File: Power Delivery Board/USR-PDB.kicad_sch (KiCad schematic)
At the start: 32 parts, among them U1 XT90, U10 Anderson PP45 Vert. 2x1, U11 Anderson PP45 Vert. 2x1, U12 TL2575HV-05IKV, U13 MCP3002-I/P, U2 LM2676T-12_NOPB, U5 Anderson PP45 Vert. 2x1, U6 Anderson PP45 Vert. 2x1, U7 Anderson PP45 Vert. 2x1, U8 Anderson PP45 Vert. 2x1, U9 Anderson PP45 Vert. 2x1

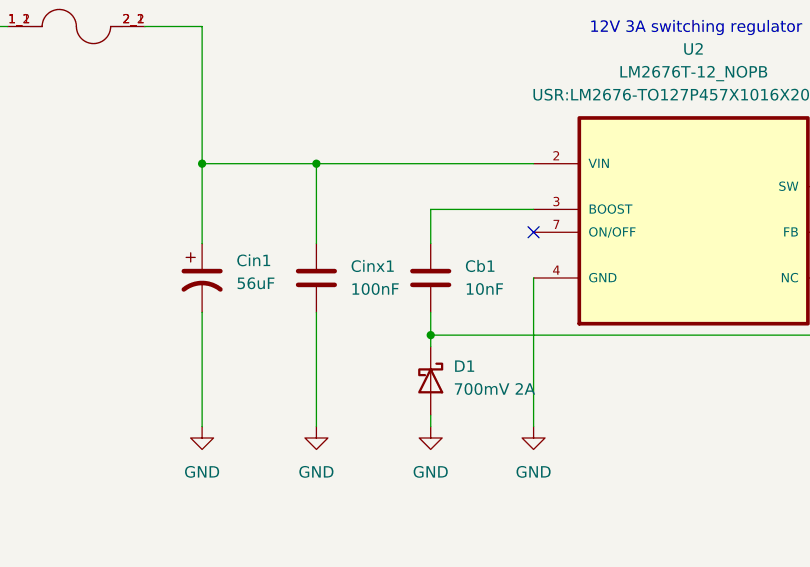
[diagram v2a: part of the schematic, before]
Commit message: Added footprints and datasheets for capacitors, inductors, and diodes
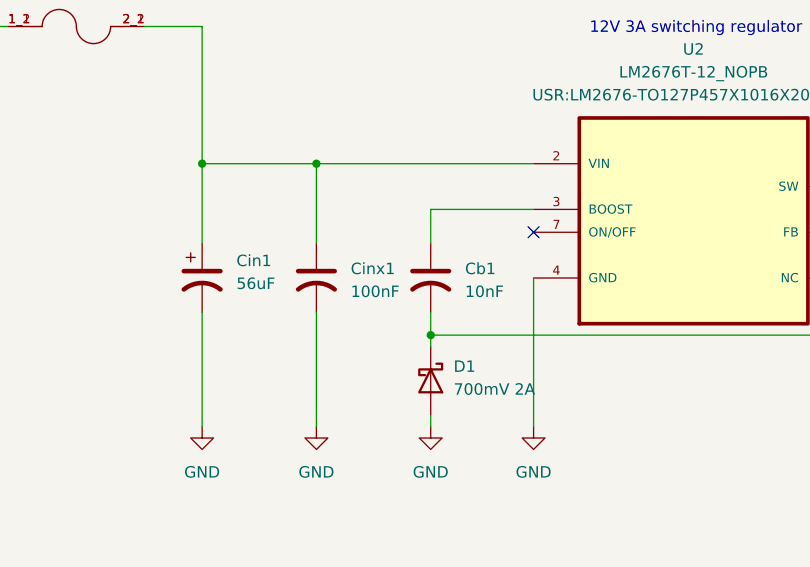
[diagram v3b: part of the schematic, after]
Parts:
- C1, C3: footprint (none) -> USR:U2-K_NCH
- C2: footprint (none) -> USR:PCAP_6.3x7.7-ELECT_NCA
- Cb1, Cinx1: footprint (none) -> USR:CAP_C320C_MOLDED RADIAL_KEM; symbol Device:C -> Device:C_US
- Cin1: footprint (none) -> USR:CAP_WCAP-ATUL_05.0X11.0_WRE
- Cout1: footprint (none) -> USR:CAP_ATLL_06p3X15p0_WRE
- D1: footprint (none) -> USR:SMA_DIO
- L1: footprint (none) -> USR:IND_BOURNS_SRR1210
- L2: footprint (none) -> USR:IND_BOURNS_SDR1806
- L3: footprint (none) -> USR:WE-FI_7447025
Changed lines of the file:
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@@
 			)
 		)
-		(property "Footprint" ""
+		(property "Footprint" "USR:CAP_ATLL_06p3X15p0_WRE"
 			(at 152.4 204.47 0)
 			(effects
@@
 			)
 		)
-		(property "Datasheet" "~"
+		(property "Datasheet" "https://www.we-online.com/components/products/datasheet/860160673019.pdf"
 			(at 152.4 204.47 0)
 			(effects
@@
 			)
 		)
-		(property "Footprint" ""
+		(property "Footprint" "USR:WE-FI_7447025"
 			(at 361.95 210.82 0)
 			(effects
@@
 			)
 		)
-		(property "Footprint" ""
+		(property "Footprint" "USR:PCAP_6.3x7.7-ELECT_NCA"
 			(at 316.23 227.33 0)
 			(effects
@@
 			)
 		)
-		(property "Footprint" ""
+		(property "Footprint" "USR:CAP_WCAP-ATUL_05.0X11.0_WRE"
 			(at 63.5 204.47 0)
 			(effects
@@
 			)
 		)
-		(property "Datasheet" "~"
+		(property "Datasheet" "https://www.we-online.com/components/products/datasheet/860040472002.pdf"
 			(at 63.5 204.47 0)
 			(effects
@@
 			)
 		)
-		(property "Footprint" ""
+		(property "Footprint" "USR:U2-K_NCH"
 			(at 267.97 208.28 0)
 			(effects
@@
 			)
 		)
-		(property "Datasheet" "~"
+		(property "Datasheet" "https://www.nichicon.co.jp/english/series_items/catalog_pdf/e-uud.pdf"
 			(at 267.97 208.28 0)
 			(effects
@@
 	)
 	(symbol
-		(lib_id "Device:C")
+		(lib_id "Device:C_US")
 		(at 88.9 204.47 0)
 		(unit 1)
@@
 		(fields_autoplaced yes)
 		(property "Reference" "Cb1"
-			(at 92.71 203.1999 0)
+			(at 92.71 203.4539 0)
 			(effects
 				(font
@@
 		)
 		(property "Value" "10nF"
-			(at 92.71 205.7399 0)
+			(at 92.71 205.9939 0)
 			(effects
 				(font
@@
 			)
 		)
-		(property "Footprint" ""
-			(at 89.8652 208.28 0)
+		(property "Footprint" "USR:CAP_C320C_MOLDED RADIAL_KEM"
+			(at 88.9 204.47 0)
 			(effects
 				(font
@@
 			)
 		)
-		(property "Datasheet" "~"
+		(property "Datasheet" "https://content.kemet.com/datasheets/KEM_C1049_GOLDMAX_C0G.pdf"
 			(at 88.9 204.47 0)
 			(effects
@@
 			)
 		)
-		(property "Description" "Unpolarized capacitor"
+		(property "Description" "capacitor, US symbol"
 			(at 88.9 204.47 0)
 			(effects
@@
 			)
 		)
-		(property "Footprint" ""
+		(property "Footprint" "USR:SMA_DIO"
 			(at 88.9 215.9 0)
 			(effects
@@
 			)
 		)
-		(property "Footprint" ""
+		(property "Footprint" "USR:U2-K_NCH"
 			(at 370.84 220.98 0)
 			(effects
@@
 			)
 		)
-		(property "Datasheet" "~"
+		(property "Datasheet" "https://www.nichicon.co.jp/english/series_items/catalog_pdf/e-uud.pdf"
 			(at 370.84 220.98 0)
 			(effects
@@
 			)
 		)
-		(property "Footprint" ""
+		(property "Footprint" "USR:IND_BOURNS_SDR1806"
 			(at 298.45 215.9 0)
 			(effects
@@
 			)
 		)
-		(property "Footprint" ""
+		(property "Footprint" "USR:IND_BOURNS_SRR1210"
 			(at 147.32 194.31 0)
 			(effects
@@
 	)
 	(symbol
-		(lib_id "Device:C")
+		(lib_id "Device:C_US")
 		(at 76.2 204.47 0)
 		(unit 1)
@@
 		(fields_autoplaced yes)
 		(property "Reference" "Cinx1"
-			(at 80.01 203.1999 0)
+			(at 80.01 203.4539 0)
 			(effects
 				(font
@@
 		)
 		(property "Value" "100nF"
-			(at 80.01 205.7399 0)
+			(at 80.01 205.9939 0)
 			(effects
 				(font
@@
 			)
 		)
-		(property "Footprint" ""
-			(at 77.1652 208.28 0)
+		(property "Footprint" "USR:CAP_C320C_MOLDED RADIAL_KEM"
+			(at 76.2 204.47 0)
 			(effects
 				(font
@@
 			)
 		)
-		(property "Description" "Unpolarized capacitor"
+		(property "Description" "capacitor, US symbol"
 			(at 76.2 204.47 0)
 			(effects

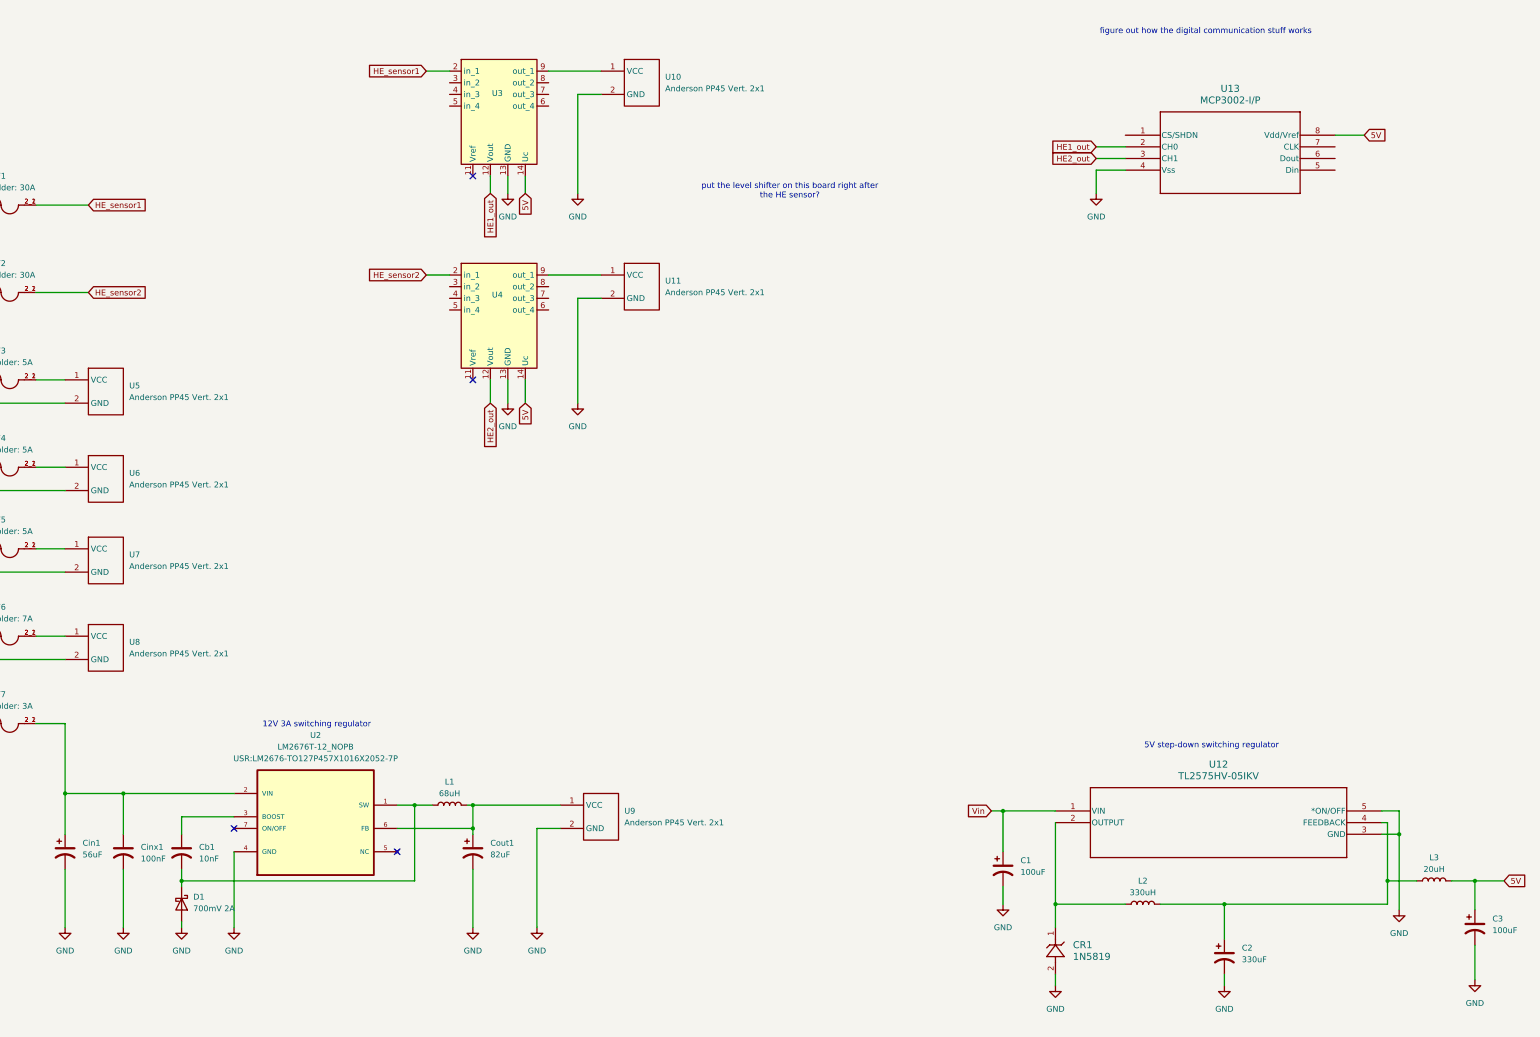
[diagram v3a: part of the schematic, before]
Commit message: adjusted PCB layout for Power delivery board
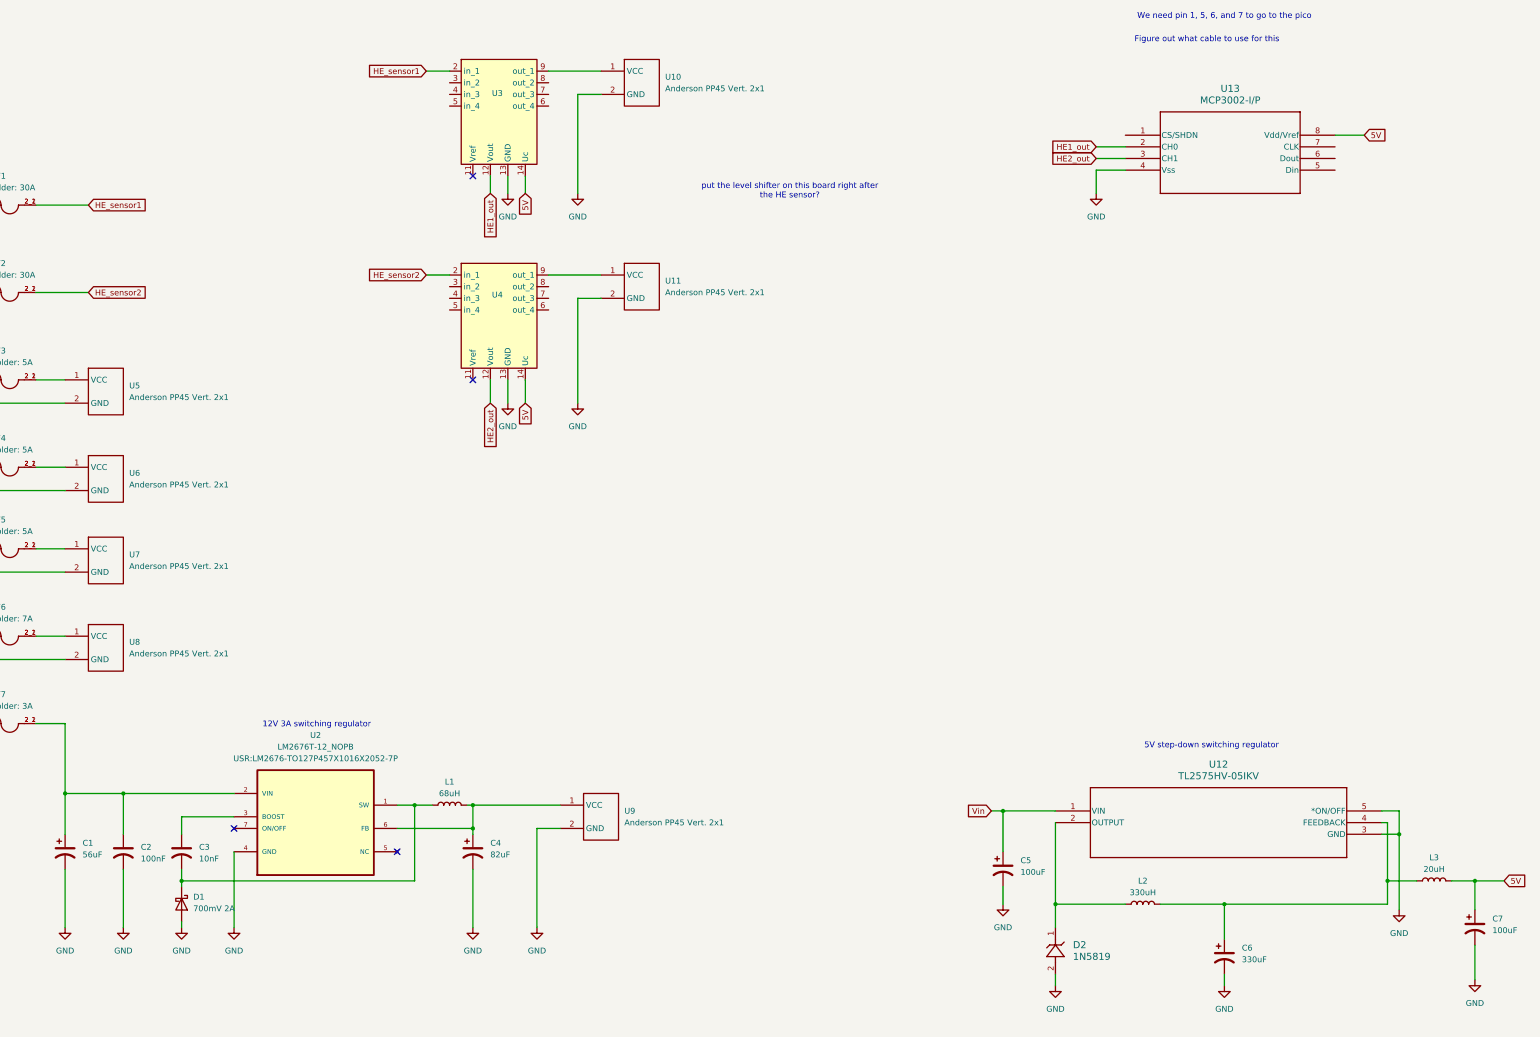
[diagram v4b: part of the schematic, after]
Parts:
- renumbered Cin1 to C1, Cinx1 to C2, Cb1 to C3, Cout1 to C4, C1 to C5, C2 to C6, C3 to C7, CR1 to D2
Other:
- note added: "Figure out what cable to use for this"
- note added: "We need pin 1, 5, 6, and 7 to go to the pico"
- note removed: "figure out how the digital communication stuff works"
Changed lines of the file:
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@@
 		)
 	)
-	(text "figure out how the digital communication stuff works\n"
+	(text "Figure out what cable to use for this\n\n"
 		(exclude_from_sim no)
-		(at 312.166 25.654 0)
+		(at 312.42 28.448 0)
 		(effects
 			(font
@@
 		)
 	)
+	(text "We need pin 1, 5, 6, and 7 to go to the pico"
+		(exclude_from_sim no)
+		(at 316.23 22.352 0)
+		(effects
+			(font
+				(size 1.27 1.27)
+			)
+		)
+	)
 	(text "12V 3A switching regulator\n"
 		(exclude_from_sim no)
@@
 		(dnp no)
 		(fields_autoplaced yes)
-		(property "Reference" "Cout1"
+		(property "Reference" "C4"
 			(at 156.21 202.5649 0)
 			(effects
@@
 			(project "USR-PDB"
 				(path "/f68b009f-fb0c-4740-82e4-ffb6e04b94c2"
-					(reference "Cout1")
+					(reference "C4")
 					(unit 1)
 				)
@@
 		(dnp no)
 		(fields_autoplaced yes)
-		(property "Reference" "C2"
+		(property "Reference" "C6"
 			(at 320.04 225.4249 0)
 			(effects
@@
 			(project "USR-PDB"
 				(path "/f68b009f-fb0c-4740-82e4-ffb6e04b94c2"
-					(reference "C2")
+					(reference "C6")
 					(unit 1)
 				)
@@
 		(dnp no)
 		(fields_autoplaced yes)
-		(property "Reference" "CR1"
+		(property "Reference" "D2"
 			(at 283.21 224.7899 90)
 			(effects
@@
 			(project ""
 				(path "/f68b009f-fb0c-4740-82e4-ffb6e04b94c2"
-					(reference "CR1")
+					(reference "D2")
 					(unit 1)
 				)
@@
 		(dnp no)
 		(fields_autoplaced yes)
-		(property "Reference" "Cin1"
+		(property "Reference" "C1"
 			(at 67.31 202.5649 0)
 			(effects
@@
 			(project ""
 				(path "/f68b009f-fb0c-4740-82e4-ffb6e04b94c2"
-					(reference "Cin1")
+					(reference "C1")
 					(unit 1)
 				)
@@
 		(dnp no)
 		(fields_autoplaced yes)
-		(property "Reference" "C1"
+		(property "Reference" "C5"
 			(at 271.78 206.3749 0)
 			(effects
@@
 			(project ""
 				(path "/f68b009f-fb0c-4740-82e4-ffb6e04b94c2"
-					(reference "C1")
+					(reference "C5")
 					(unit 1)
 				)
@@
 		(dnp no)
 		(fields_autoplaced yes)
-		(property "Reference" "Cb1"
+		(property "Reference" "C3"
 			(at 92.71 203.4539 0)
 			(effects
@@
 			(project "USR-PDB"
 				(path "/f68b009f-fb0c-4740-82e4-ffb6e04b94c2"
-					(reference "Cb1")
+					(reference "C3")
 					(unit 1)
 				)
@@
 		(dnp no)
 		(fields_autoplaced yes)
-		(property "Reference" "C3"
+		(property "Reference" "C7"
 			(at 374.65 219.0749 0)
 			(effects
@@
 			(project "USR-PDB"
 				(path "/f68b009f-fb0c-4740-82e4-ffb6e04b94c2"
-					(reference "C3")
+					(reference "C7")
 					(unit 1)
 				)
@@
 		(dnp no)
 		(fields_autoplaced yes)
-		(property "Reference" "Cinx1"
+		(property "Reference" "C2"
 			(at 80.01 203.4539 0)
 			(effects
@@
 			(project ""
 				(path "/f68b009f-fb0c-4740-82e4-ffb6e04b94c2"
-					(reference "Cinx1")
+					(reference "C2")
 					(unit 1)
 				)

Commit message: added SYM & footprint for JST connectors, added comments to PDB schem
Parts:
- added F8: Extra fuse holder, USR:FUSE_3557-15, symbol USR:3557-15
- added U14: Anderson PP45 Vert. 2x1, USR:ANDERSON PP45 VERT. 2X1, symbol USR:root_0_Anderson_PP45_Vert._2x1_
- added U15: ~, USR:JST-XA 2.54mm, symbol USR:JST-XA
- D1: value 700mV 2A -> B220/A
- U13: symbol USR_SymLibrary:MCP3002-I_P -> USR:MCP3002-I_P
- U3, U4: symbol USR_SymLibrary:LKSR_50-NP -> USR:LKSR_50-NP
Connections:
- net GND: now also U14.2 (GND)
- net Vin: now also F8.1_1, F8.1_2
- new net: F8.2_1, F8.2_2, U14.1 (VCC)
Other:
- note added: "conformal coating [look into this for the pcb]"
- note added: "connect the pins like this GND - 5V - GND"
- note added: "create a vertical version of the AMASS_XT90PW-M for the hole sizes, reference the AMASS_XT30 vertical footprint for the layout we want"
- note added: "find XT90 footprint"
- note added: "look into using JST 2.54mm XA male connectors for this"
- note added: "try and make specific values out of equivalent values"
- note added: "use 10uH 0805 inductors, combine them into the 20uH inductor here"
- note added: "use the 0805 SMD cap's we already have for the 100nF and 10nF cap's"
- note added: "use the 3-pin JST-XA connectors to route 5V to the backplane"
- note removed: "Figure out what cable to use for this"
- moved on the sheet: C1, C2, C3, C4, D1, F7, L1, U2, U9

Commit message: updated PDB schematic
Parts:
- added C2: 100uF, USR:U2-K_NCH, symbol Device:C_Polarized_US
- added L3: 100uH, USR:IND_BOURNS_SDR1806, symbol Device:L
- added L4, L6: 10uH, Inductor_SMD:L_0805_2012Metric_Pad1.05x1.20mm_HandSolder, symbol Device:L
- added U16: ~, USR:JST-XA 3-PIN, symbol USR:JST-XA_3-PIN
- C1: value 56uF -> 100uF
- C3: renamed from C2; footprint USR:CAP_C320C_MOLDED RADIAL_KEM -> Capacitor_SMD:C_0805_2012Metric_Pad1.18x1.45mm_HandSolder
- C4: renamed from C3; footprint USR:CAP_C320C_MOLDED RADIAL_KEM -> Capacitor_SMD:C_0805_2012Metric_Pad1.18x1.45mm_HandSolder
- C5: renamed from C4; value 82uF -> 100uF
- D1: value B220/A -> 1N5821
- D2: symbol USR:1N5819 -> Device:D_Schottky
- L2: value 330uH -> 220uH
- L5: renamed from L3; value 20uH -> 10uH; footprint USR:WE-FI_7447025 -> Inductor_SMD:L_0805_2012Metric_Pad1.05x1.20mm_HandSolder
- renumbered C5 to C6, C6 to C7, C7 to C8, F8 to F7, F7 to F8, U9 to U10, U10 to U11, U11 to U12, U12 to U13, U13 to U14, U5 to U2, U6 to U3, U7 to U4, U8 to U5, U14 to U6, U2 to U7, U3 to U8, U4 to U9
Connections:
- net 5V: now also L6.2, U16.2; no longer L5.2
- net GND: now also C2.2, U16.1, U16.3; no longer C1.2
- net at C7.1, L5.1, U13.4 (FEEDBACK): now also L4.2; no longer L2.2
- net CS: now reaches U15.1
- net CS: now also U14.1 (CS/SHDN)
- net CLK: now reaches U15.2
- net CLK: now also U14.7 (CLK)
- net Dout: now reaches U15.3
- net Dout: now also U14.6 (Dout)
- net Din: now reaches U15.4
- net Din: now also U14.5 (Din)
- new net: L5.2, L6.1
- new net: C1.2, C2.1
- new net: L3.2, L4.1
- new net: L2.2, L3.1
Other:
- note added: "3/12/2026"
- note added: "Peter Burt"
- note added: "Things the stockroom has: - 1N5819 schottky diode - 1N5821 schottky diode - 100uF 50V caps - 330uF 35V caps - 68uH ind - 220uH, 100uH ind"
- note added: "ideal (C1 + C2), C5 values: - (C1 + C2) = 56uF - C4 = 82uF generalized (C1 + C2), C5 values: - (C1 + C2) = 50uF - C4 = 100uF"
- note removed: "2/5/2026"
- note removed: "try and make specific values out of equivalent values"
- moved on the sheet: C1, C8, L2, L5, U15
